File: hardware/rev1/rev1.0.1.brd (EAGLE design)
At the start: 58.1 x 44.9 mm, 42 parts, among them Q1 MOSFET-NCHANNEL-IRLR3705ZPBF, Q2 MOSFET-PCHANNEL, Q3 MOSFET-NCHANNELBSS138, U1 ATMEGA168-AU, U2 5v, U3 74AHC1G04DBV, Y1 16MHz

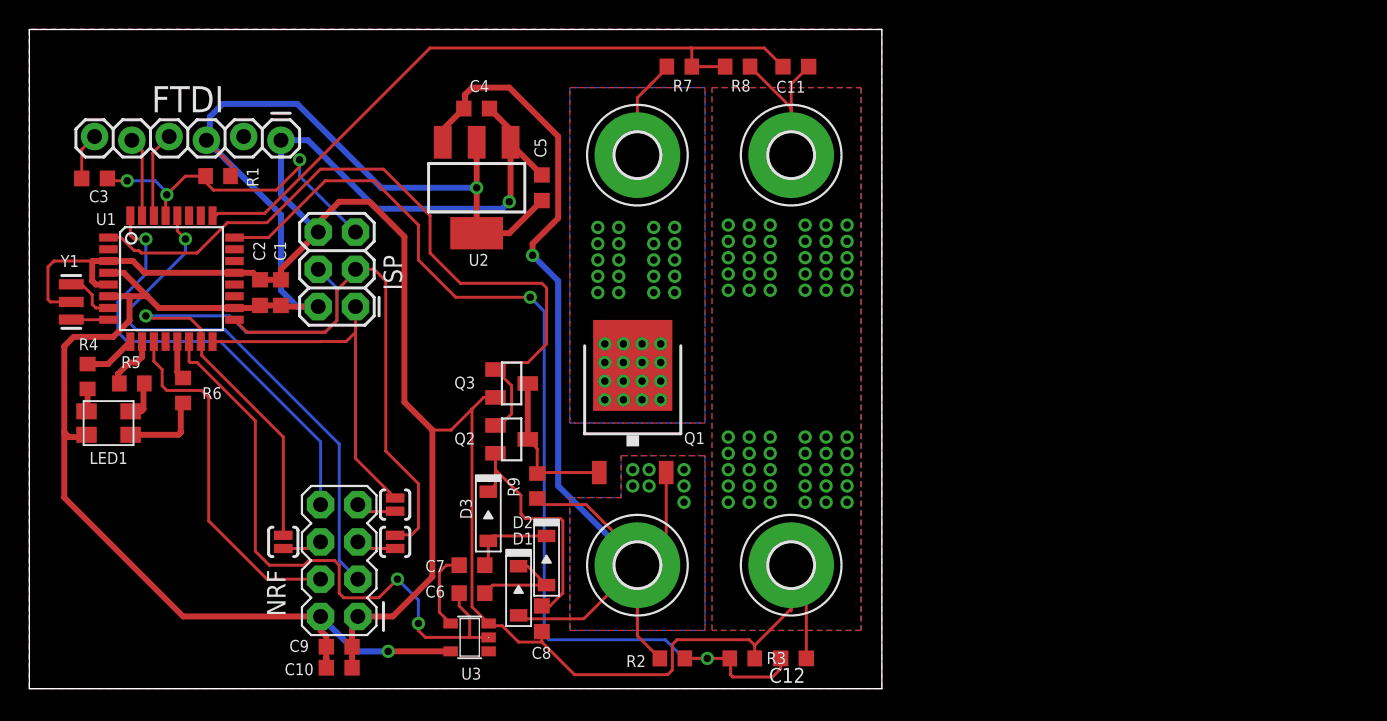
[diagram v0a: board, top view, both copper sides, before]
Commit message: Propperly filtered AVCC
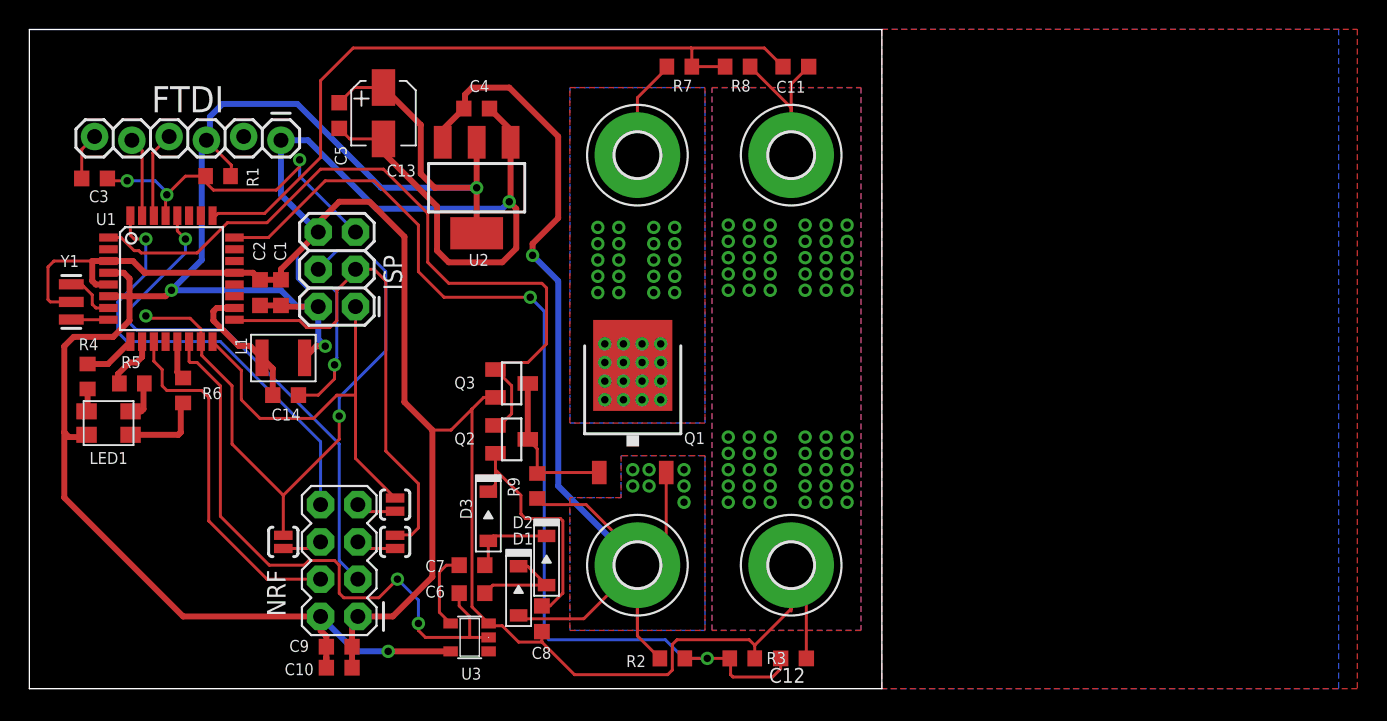
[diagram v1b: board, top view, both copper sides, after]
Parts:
- added C13: (no value), MF_Passives:CP4MM
- added C14: 0.1uF, resistor:C0603K
- added L1: 10uH, MF_Passives:L1210
- C4: value 1uF -> 10nF
- moved C5 14.7 mm to (21.1, 39.1), turned to 270 degrees
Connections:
- new net N$14: C14.1, L1.P$2, U1.18
- net +5V: now also C13.P$1, L1.P$1; no longer U1.18
- net GND: now also C13.P$2, C14.2
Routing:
- net GND: track 183.8 -> 218.4 mm, vias 61 -> 62
- net +5V: track 124.8 -> 138.5 mm, vias 2 -> 4
- net N$14: track 0.00 -> 9.37 mm
- net MOSI: track 38.3 -> 44.4 mm, vias 1 -> 2
- net MISO: track 24.2 -> 27.9 mm
- net VIN-READ: track 47.7 -> 50.8 mm
- added copper zone on layer 1, net GNDD
- added copper zone on layer 16, net GNDD
